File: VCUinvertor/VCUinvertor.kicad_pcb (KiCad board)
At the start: 2 copper layers, 97.3 x 113.8 mm, 97 parts, among them J7 PowerSupply, J8 CAN_NXP, J9 BACKLIGHT, Q1 2N7002, Q10 2N7002, Q2 2N7002, Q3 2N7002, Q4 2N7002, Q5 2N7002, Q6 2N7002, Q7 2N7002, Q8 2N7002, Q9 2N7002, U1 TJA1448ATK, U2 REF3433T, U3 TLV76150DCY

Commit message: LastCorrection_ToBeChecked
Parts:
- C1, C11, C5, C6: moved to B.Cu
- C3, C4, D1, U3: moved to F.Cu
- J7: footprint Connector_Phoenix_MSTB:PhoenixContact_MSTBVA_2,5_2-G-5,08_1x02_P5.08mm_Vertical -> Connector_JST:JST_PH_B2B-PH-K_1x02_P2.00mm_Vertical
- JO1: value -PWR (Pink) -> PWR (Pink)
- JO11: value -ECO (Blue) -> ECO (Blue)
- JO12: value -TPS (Green) -> TPS (Green)
- JO13: value -5V (Purple) -> 5V (Purple)
- JO14, JO6: value -GND (Black) -> GND (Black)
- JO15, JO4: value -12V (Red) -> 12V (Red)
- JO19: value -ACC (Gray) -> ACC (Gray)
- JO3: value -REV (Orange) -> REV (Orange)
- JO5: value -FWD (White) -> FWD (White)
- JO9: value -H_Brk (Yellowish) -> H_Brk (Yellowish)
- moved C2 20.2 mm to (86.2, 93.2), turned to -90 degrees
- moved C5 17.5 mm to (98.5, 89.4), turned to 90 degrees
- moved R26 15.1 mm to (105.5, 87.6), turned to 90 degrees
- moved U2 14.8 mm to (89.0, 93.3), turned to -90 degrees
- moved C6 11.8 mm to (102.3, 94.0), turned to 0 degrees
- moved R25 11.5 mm to (105.5, 91.0), turned to 90 degrees
- moved C11 9.46 mm to (91.1, 91.5), turned to 90 degrees
- moved D1 8.54 mm to (99.4, 64.0)
- moved J7 7.48 mm to (133.5, 50.8), turned to 90 degrees
- moved C1 4.61 mm to (99.9, 98.7)
- moved C4 4.59 mm to (104.8, 69.9), turned to 0 degrees
- moved JO10 4.44 mm to (145.4, 111.9)
- moved R28 4.40 mm to (94.8, 88.4), turned to 90 degrees
- moved JO12 4.36 mm to (141.6, 114.0)
- moved R27 4.08 mm to (94.8, 91.8), turned to 90 degrees
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- renumbered J8 to J21
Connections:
- net /CAN_H renamed Net-(CA1-Pin_1)
- net /CAN_L renamed Net-(CA1-Pin_2)
- net NXP_TPS01 renamed /TPS1
- net NXP_TPS02 renamed /TPS2
- NXP11 pad 16: unconnected-(NXP11-Pin_16-Pad16) -> /Pyy
- NXP11 pad 4: unconnected-(NXP11-Pin_4-Pad4) -> /Pzz
- NXP15 pad 11: /PWM_NXP2 -> /PWM_NXP1
- NXP15 pad 9: /PWM_NXP1 -> /PWM_NXP2
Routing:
- net +12V: track 269.5 -> 235.8 mm
- net /Pyy: track 0.00 -> 23.7 mm, vias 0 -> 1
- net /Pzz: track 0.00 -> 22.0 mm, vias 0 -> 2
- net /TPS2: track 52.6 -> 63.1 mm
- net +5V: track 90.7 -> 97.6 mm
- net /PWM_NXP2: track 50.5 -> 46.5 mm
- net GND: track 54.3 -> 58.1 mm, vias 18 -> 20
- net /PWM_NXP4: track 50.4 -> 54.1 mm
- net /Brk_AN2: track 45.2 -> 48.3 mm
- net /Brk_AN1: track 49.5 -> 51.9 mm
- net /TX1: track 46.6 -> 48.7 mm
- net +3.3V: track 60.0 -> 58.1 mm, vias 4 -> 5
- net /PWM_NXP3: track 51.2 -> 52.4 mm, vias 2 -> 0
- net NXP_TPSOUT01: track 44.4 -> 45.6 mm, vias 1 -> 2
- net /NXP_ECO02: track 11.7 -> 12.9 mm
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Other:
- board text added: "12V (Red)"
- board text added: "5V (Purple)"
- board text added: "ACC (Gray)"
- board text added: "Brk_AN (Brown)"
- board text added: "CAN_H (Greenish)"
- board text added: "CAN_L (Brownish)"
- board text added: "ECO (Blue)"
- board text added: "FWD (White)"
- board text added: "GND (Black)"
- board text added: "H_Brk (Yellowish)"
- board text added: "PWR (Pink)"
- board text added: "REV (Orange)"
- board text added: "TPS (Green)"

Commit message: Logo_added
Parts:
- added G***: LOGO, LOGO, F.Cu at (79.3, 148.5)
- added G***: LOGO, LOGO, F.Cu at (78.4, 139.5)
- moved C3 14.3 mm to (99.4, 71.8)
- moved U3 13.9 mm to (99.6, 77.2)
- moved D1 13.9 mm to (94.7, 77.1)
- moved C4 13.6 mm to (100.1, 82.6)
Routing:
- net +12V: track 235.8 -> 253.8 mm
- net +5V: track 97.6 -> 82.5 mm
- net /Pzz: track 22.0 -> 22.9 mm
- net /CANH01: track 18.4 -> 18.9 mm
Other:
- board text added: "C3"

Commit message: Block diagram cleanup
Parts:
- J9: value BACKLIGHT -> BREAKLIGHT
- JO21: value -PWR (Pink) -> PWR (Pink)
- JO22: value -REV (Orange) -> REV (Orange)
- JO23: value -FWD (White) -> FWD (White)
- JO24, JO35: value -12V (Red) -> 12V (Red)
- JO25: value -H_Brk (Yellowish) -> H_Brk (Yellowish)
- JO26, JO34: value -GND (Black) -> GND (Black)
- JO29: value -ECO (Blue) -> ECO (Blue)
- JO31: value -ACC (Gray) -> ACC (Gray)
- JO32: value -TPS (Green) -> TPS (Green)
- JO33: value -5V (Purple) -> 5V (Purple)
- renumbered J21 to CA0
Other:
- outline, holes or cut-outs redrawn

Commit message: BOM csv added
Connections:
- JU1 pad MP: (no net) -> GND
- JU2 pad MP: (no net) -> GND
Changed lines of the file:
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@@
 	)
 	(footprint "Connector_JST:JST_GH_SM04B-GHS-TB_1x04-1MP_P1.25mm_Horizontal"
-		(locked yes)
 		(layer "B.Cu")
 		(at 99.93 148.300001 180)
@@
 			(layers "B.Cu" "B.Mask" "B.Paste")
 			(roundrect_rratio 0.25)
+			(net 30 "GND")
+			(pinfunction "MP")
+			(pintype "passive")
 		)
 		(pad "MP" smd roundrect
@@
 			(layers "B.Cu" "B.Mask" "B.Paste")
 			(roundrect_rratio 0.25)
+			(net 30 "GND")
+			(pinfunction "MP")
+			(pintype "passive")
 		)
 		(embedded_fonts no)
@@
 	)
 	(footprint "Connector_JST:JST_GH_SM04B-GHS-TB_1x04-1MP_P1.25mm_Horizontal"
-		(locked yes)
 		(layer "B.Cu")
 		(at 112.5 148.14 180)
@@
 			(layers "B.Cu" "B.Mask" "B.Paste")
 			(roundrect_rratio 0.25)
+			(net 30 "GND")
+			(pinfunction "MP")
+			(pintype "passive")
 		)
 		(pad "MP" smd roundrect
@@
 			(layers "B.Cu" "B.Mask" "B.Paste")
 			(roundrect_rratio 0.25)
+			(net 30 "GND")
+			(pinfunction "MP")
+			(pintype "passive")
 		)
 		(embedded_fonts no)
@@
 	)
 	(group ""
-		(locked yes)
-		(members "03823f51-c2e7-49cb-8d95-1b901c702bf4" "9b059115-2564-4c5e-a147-b3831b46a45a")
-	)
-	(group ""

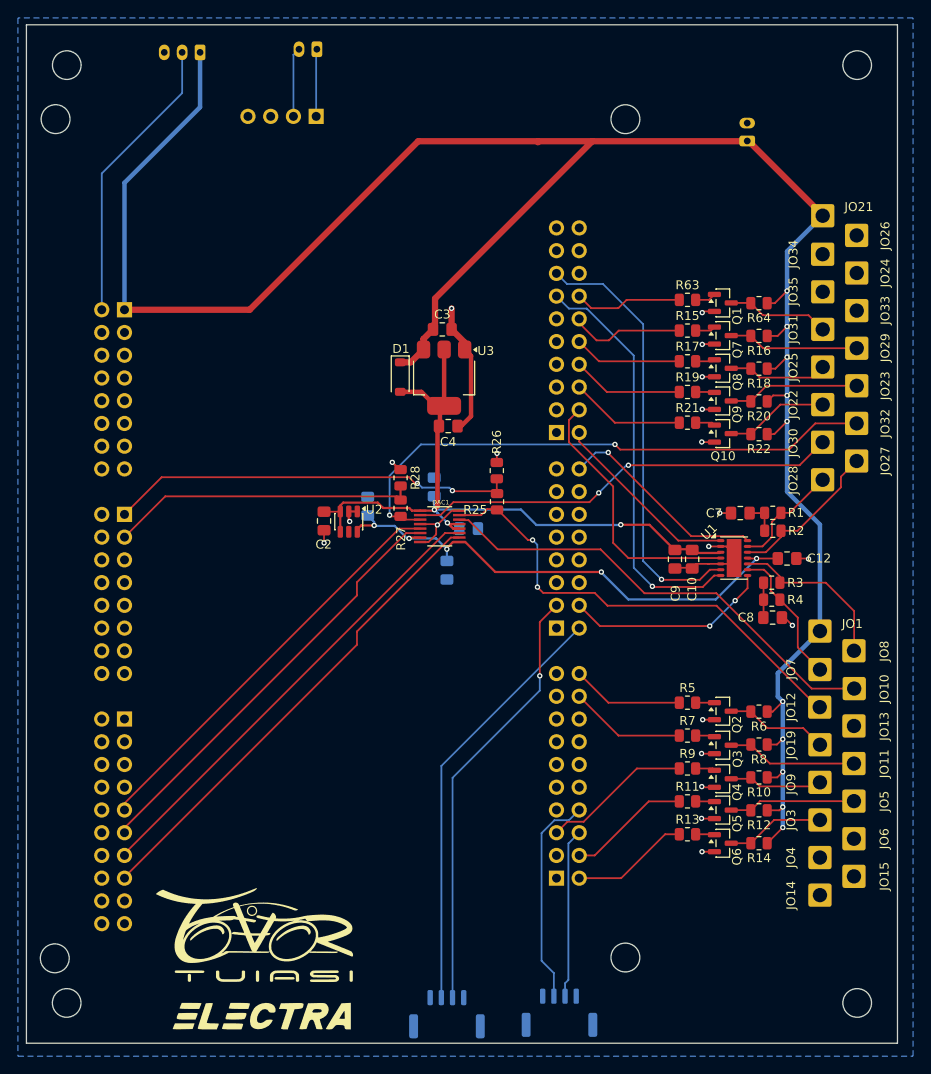
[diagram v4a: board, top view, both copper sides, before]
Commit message: Changes on Supply
1.Protection shottky diode added
2.Separate supply for INV via Darlington (1A Max.)
3.Control of the supply from J10 Pin 20 for INV supply - added
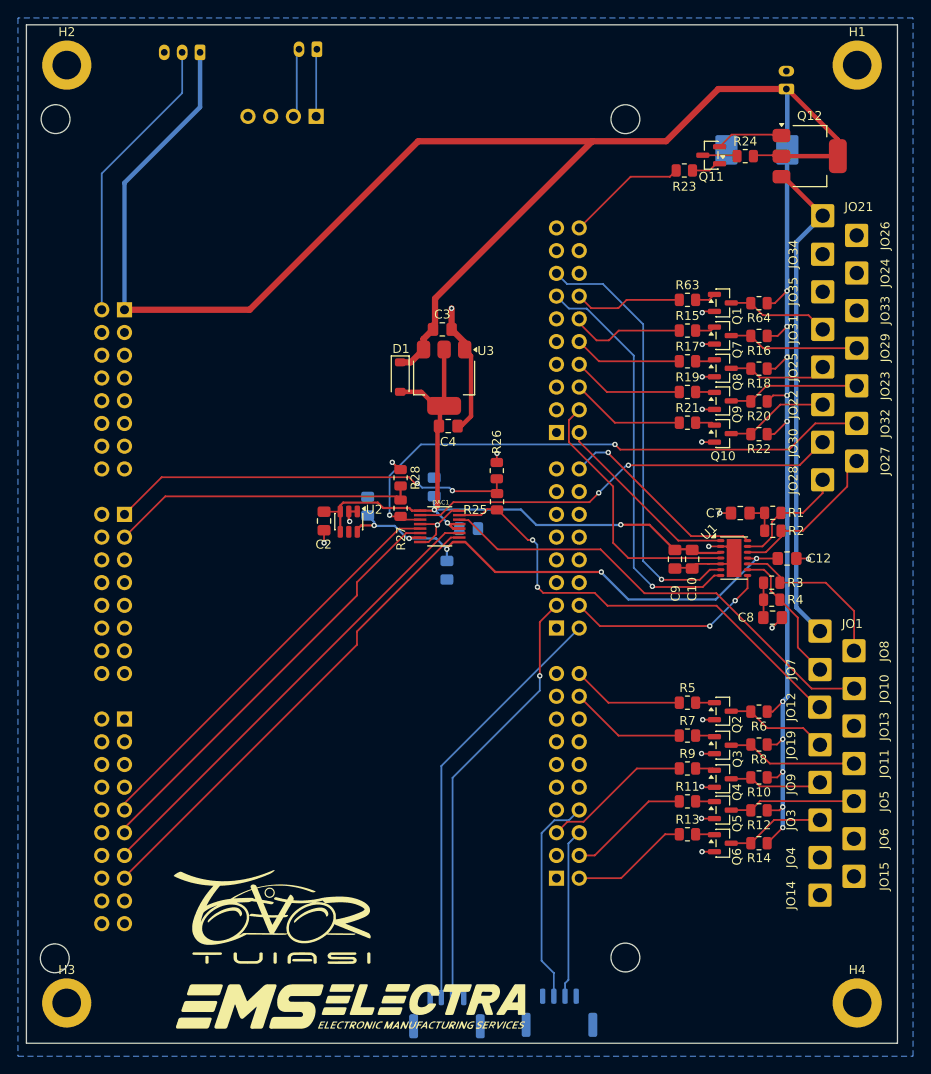
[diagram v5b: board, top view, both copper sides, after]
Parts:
- removed the G*** at (79.3, 148.5)
- added D2: MBRS340, Diode_SMD:D_SMC, B.Cu at (134.6, 51.7)
- added H1: MountingHole_Pad, MountingHole:MountingHole_3.2mm_M3_ISO14580_Pad, F.Cu at (145.8, 42.3)
- added H2: MountingHole_Pad, MountingHole:MountingHole_3.2mm_M3_ISO14580_Pad, F.Cu at (57.5, 42.3)
- added H3: MountingHole_Pad, MountingHole:MountingHole_3.2mm_M3_ISO14580_Pad, F.Cu at (57.5, 147.0)
- added H4: MountingHole_Pad, MountingHole:MountingHole_3.2mm_M3_ISO14580_Pad, F.Cu at (145.8, 147.0)
- added Q11: BC848, Package_TO_SOT_SMD:SOT-23, F.Cu at (129.5, 52.3)
- added Q12: BCP51, Package_TO_SOT_SMD:SOT-223-3_TabPin2, F.Cu at (140.5, 52.4)
- added R23: 10k, Resistor_SMD:R_0805_2012Metric, F.Cu at (126.5, 54.0)
- added R24: 1k, Resistor_SMD:R_0805_2012Metric, F.Cu at (133.3, 52.4)
- moved J7 7.27 mm to (137.9, 44.9)
- moved G*** 2.82 mm to (80.4, 137.4)
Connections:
- JO1 pad 1: +12V -> /INV_Supply
- JO21 pad 1: +12V -> /INV_Supply
- JO26 pad 1: unconnected-(JO26-Pin_1-Pad1) -> GND
- JO6 pad 1: unconnected-(JO6-Pin_1-Pad1) -> GND
- NXP10 pad 20: unconnected-(NXP10-Pin_20-Pad20) -> INV_OFF
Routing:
- net /INV_Supply: track 0.00 -> 55.3 mm
- net +12V: track 253.8 -> 277.0 mm
- net INV_OFF: track 0.00 -> 13.5 mm
- net Net-(Q11-E): track 0.00 -> 7.51 mm
- net Net-(Q11-C): track 0.00 -> 3.87 mm
- net Net-(Q11-B): track 0.00 -> 3.34 mm
- net /CANH02: track 12.5 -> 13.3 mm
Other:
- outline, holes or cut-outs redrawn

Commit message: BOM + Gerbers - added
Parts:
- Q11: value BC848 -> BC848C
- R23: value 10k -> 1.7k
- R24: value 1k -> 360R
- moved R24 7.14 mm to (136.8, 58.6)
- moved Q11 7.14 mm to (133.0, 58.5)
- moved R23 7.14 mm to (130.0, 60.2)
- moved J7 4.04 mm to (133.9, 44.3)
- moved Q12 1.48 mm to (139.2, 51.7), turned to 90 degrees
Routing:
- net Net-(Q11-E): track 7.51 -> 4.04 mm
- net +12V: track 277.0 -> 274.0 mm
- net /INV_Supply: track 55.3 -> 53.2 mm
- net INV_OFF: track 13.5 -> 14.5 mm

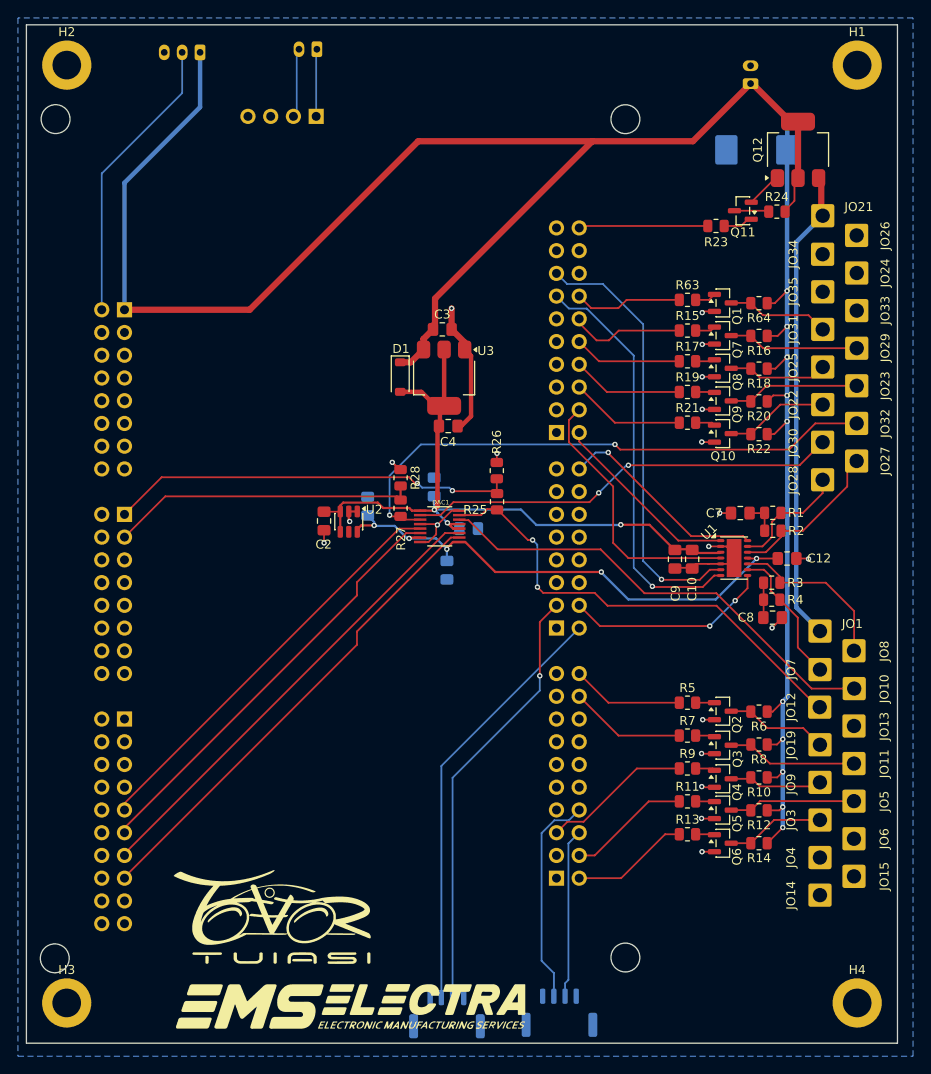
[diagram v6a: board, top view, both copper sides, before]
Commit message: SMD components resized for Handsoldering (0805 -> 1206)
*Resistors & Capacitors are now upgraded to size 1206 for easy handsoldering
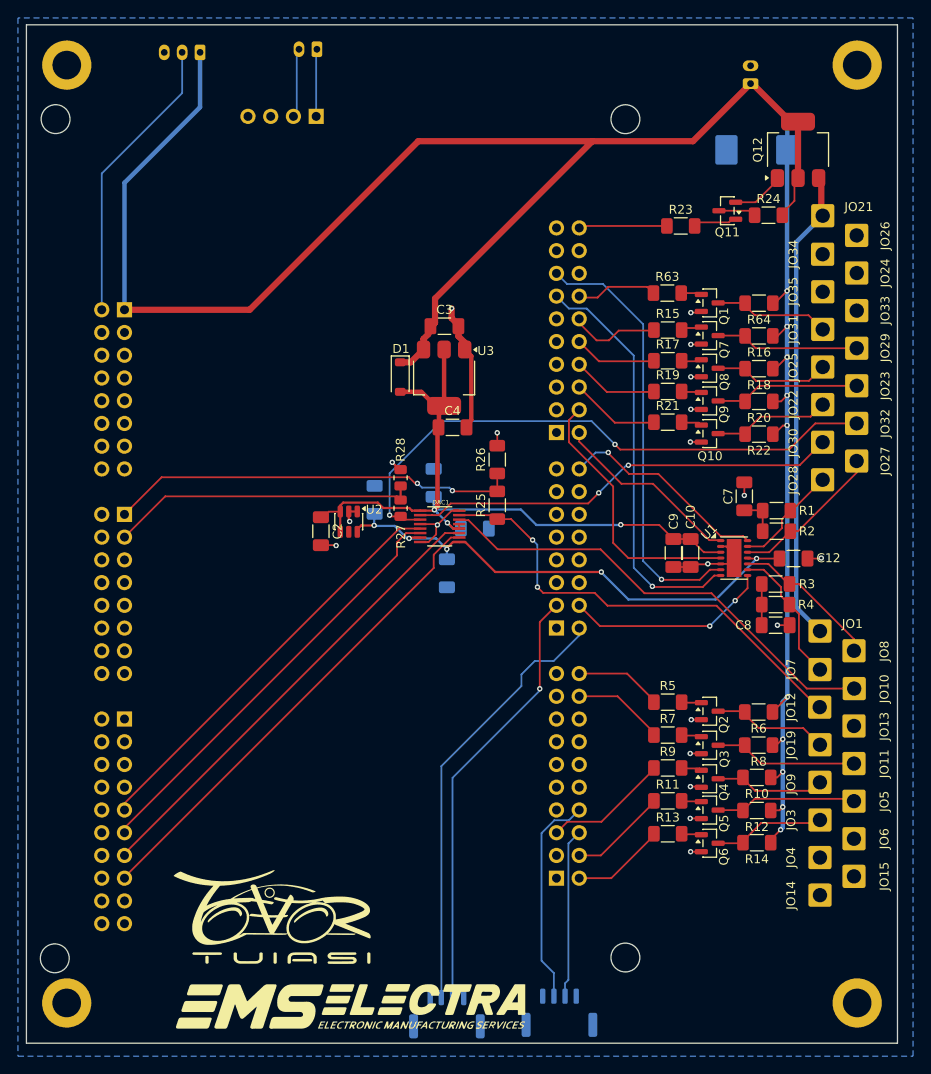
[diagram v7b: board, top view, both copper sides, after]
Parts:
- C1, C10, C11, C12, C2, C3, C4, C5, C6, C7, C8, C9: footprint Capacitor_SMD:C_0805_2012Metric_Pad1.18x1.45mm_HandSolder -> Capacitor_SMD:C_1206_3216Metric_Pad1.33x1.80mm_HandSolder
- J9: value BREAKLIGHT -> BRAKE LIGHT
- R1, R10, R11, R12, R13, R14, R15, R16, R17, R18, R19, R2, R20, R21, R22, R23, R24, R25, R26, R3, R4, R5, R6, R63, R64, R7, R8, R9: footprint Resistor_SMD:R_0805_2012Metric -> Resistor_SMD:R_1206_3216Metric_Pad1.30x1.75mm_HandSolder
- moved R23 3.94 mm to (126.1, 60.2)
- moved R63 2.37 mm to (124.6, 67.7)
- moved R15 2.20 mm to (124.6, 71.9)
- moved R11 2.20 mm to (124.6, 124.5)
- moved R17 2.20 mm to (124.6, 75.3)
- moved R19 2.20 mm to (124.6, 78.7)
- moved R21 2.20 mm to (124.6, 82.2)
- moved R5 2.20 mm to (124.6, 113.4)
- moved R7 2.20 mm to (124.6, 117.1)
- moved R9 2.20 mm to (124.6, 120.8)
- moved R13 2.20 mm to (124.6, 128.1)
- moved C7 1.93 mm to (133.2, 90.4), turned to -90 degrees
- moved Q11 1.74 mm to (131.3, 58.5)
- moved Q1 1.46 mm to (129.3, 68.8)
- moved Q10 1.46 mm to (129.3, 83.4)
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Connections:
- net BREAKLIGHT renamed BRAKELIGHT
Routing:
- net INV_OFF: track 14.5 -> 9.88 mm
- net +12V: track 274.0 -> 270.1 mm
- net /NXP_BRK02: track 12.1 -> 9.28 mm
- net /NXP_REV02: track 12.8 -> 10.0 mm
- net /NXP_FWD02: track 12.5 -> 9.65 mm
- net /NXP_ECO02: track 12.9 -> 10.1 mm
- net /NXP_ACC02: track 12.1 -> 9.35 mm
- net /NXP_ACC01: track 12.5 -> 9.79 mm
- net /NXP_BRK01: track 16.7 -> 14.0 mm
- net /NXP_FWD01: track 13.7 -> 11.0 mm
- net /NXP_ECO01: track 13.0 -> 10.3 mm
- net /NXP_REV01: track 13.2 -> 10.5 mm
- net /TPS2: track 63.1 -> 65.4 mm
- net /CANH01: track 18.9 -> 16.7 mm
- net GND: track 58.2 -> 56.2 mm
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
